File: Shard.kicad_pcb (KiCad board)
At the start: 4 copper layers, 52 parts, among them J1 USB_C_Receptacle_USB2.0_16P, J2 Conn_01x08, J3 Conn_01x08, J4 Conn_01x08, J5 Conn_01x08, SW1 SW_Push, SW2 SW_Push, U1 ESP32-S3, U2 USBLC6-2P6, U3 TLV76733DRVx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

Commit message: Finish initial PCB Layout
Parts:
- ANT1: footprint RF_Antenna:Texas_SWRA117D_2.4GHz_Left -> RF_Antenna:Texas_SWRA117D_2.4GHz_Right
- C1, C13, C15, C3, C6, C9: footprint Capacitor_SMD:C_0603_1608Metric -> Capacitor_SMD:C_0201_0603Metric
- C10, C11, C12, C16, C4, C7, C8: footprint Capacitor_SMD:C_1206_3216Metric -> Capacitor_SMD:C_0201_0603Metric
- R11: footprint Resistor_SMD:R_0805_2012Metric -> Resistor_SMD:R_0201_0603Metric
- moved J2 89.3 mm to (169.1, 81.7), turned to -20 degrees
- moved J3 87.5 mm to (168.3, 94.3), turned to -20 degrees
- moved U5 78.5 mm to (157.6, 101.0), turned to -45 degrees
- moved C16 58.2 mm to (157.3, 96.0), turned to 135 degrees
- moved Y1 57.8 mm to (151.9, 87.9), turned to -45 degrees
- moved C1 55.6 mm to (139.6, 106.7), turned to -90 degrees
- moved C20 54.9 mm to (144.4, 85.7), turned to 45 degrees
- moved R6 54.9 mm to (152.3, 97.0), turned to -45 degrees
- moved C10 54.5 mm to (148.3, 99.7), turned to -135 degrees
- moved C4 54.1 mm to (148.3, 88.6), turned to 45 degrees
- moved R7 53.6 mm to (153.4, 96.0), turned to -45 degrees
- moved R12 53.0 mm to (159.7, 95.1)
- moved R8 52.6 mm to (154.5, 94.9), turned to -45 degrees
- moved C11 52.6 mm to (151.0, 91.3), turned to 45 degrees
- moved C9 51.2 mm to (147.7, 99.1), turned to -135 degrees
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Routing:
- net VBUS: track 17.6 -> 0.00 mm
- net /D-: track 8.21 -> 0.00 mm
- net /D+: track 7.94 -> 0.00 mm
- net /D_N: track 7.79 -> 0.00 mm
- net GND: track 7.14 -> 0.00 mm, vias 1 -> 0
- net /D_P: track 7.05 -> 0.00 mm
- net Net-(J1-CC2): track 3.16 -> 0.00 mm
- net Net-(J1-CC1): track 3.16 -> 0.00 mm
- removed copper zone on F.Cu, net GND
- removed copper zone on In1.Cu, net GND

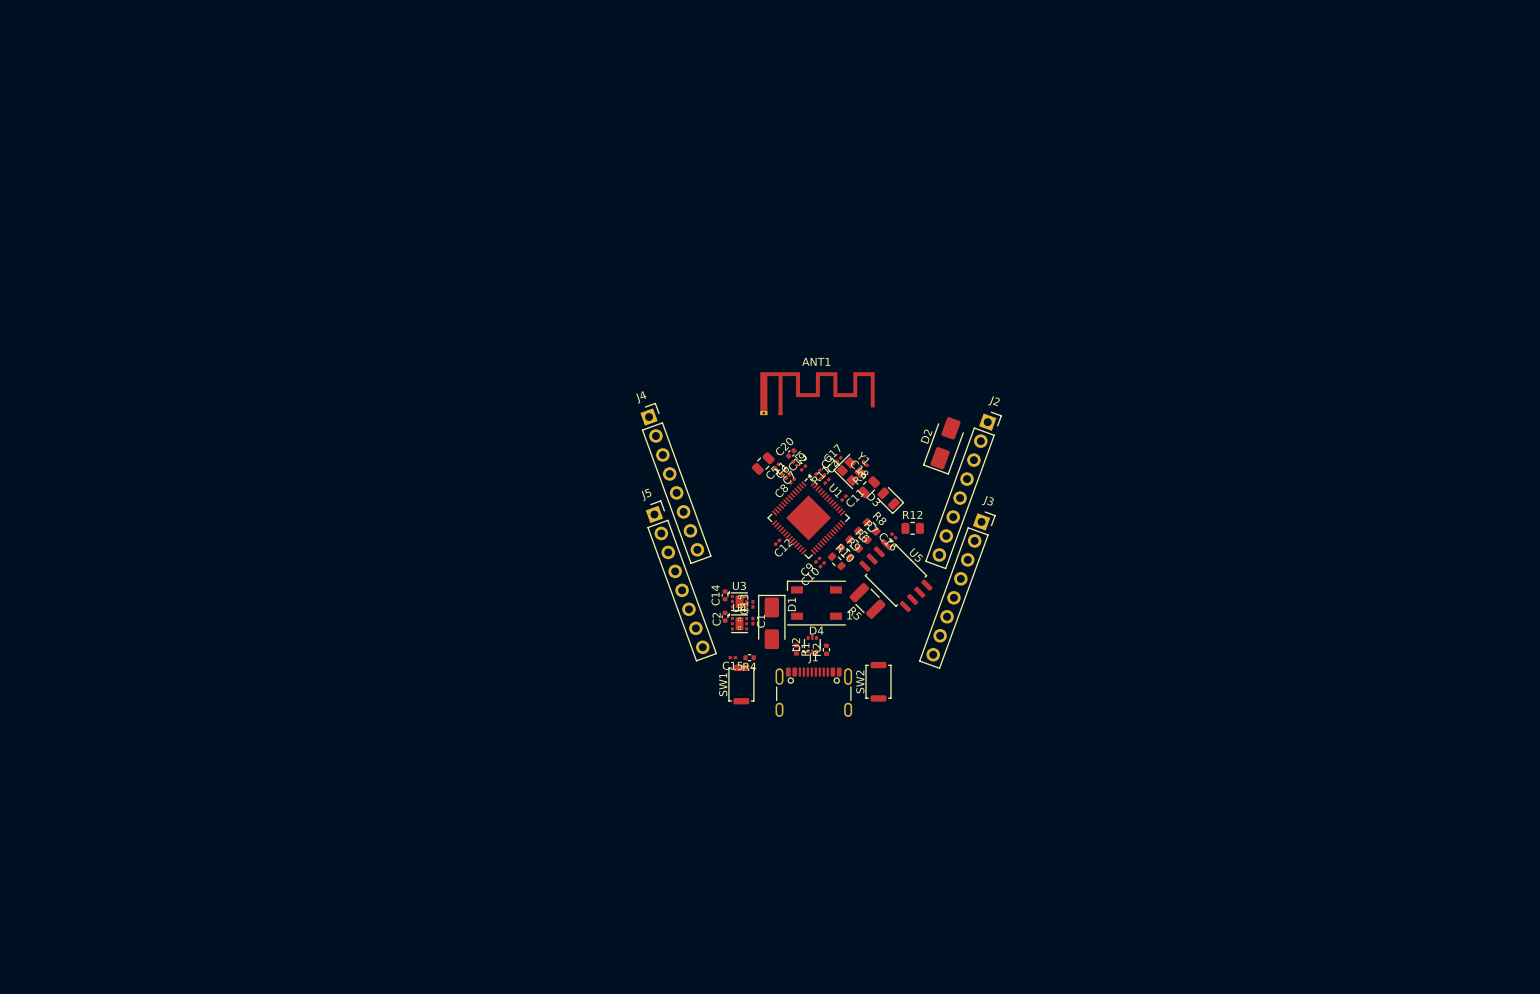
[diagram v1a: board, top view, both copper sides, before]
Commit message: Started routing USB & Power
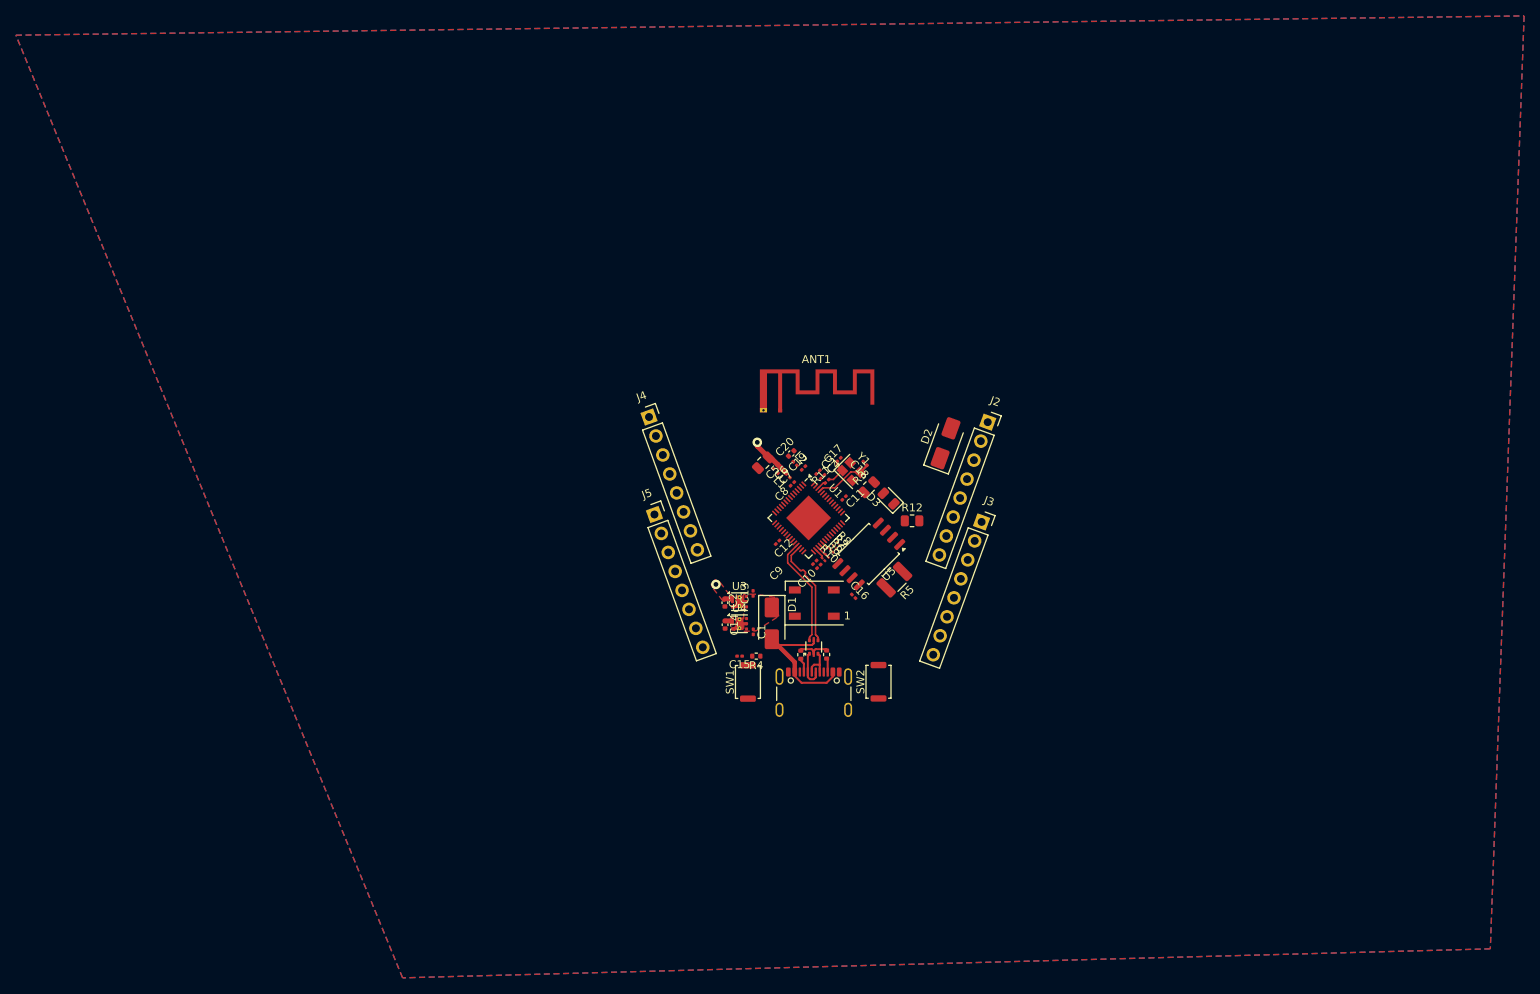
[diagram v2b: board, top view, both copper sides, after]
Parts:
- R10, R6, R7, R8, R9: footprint Resistor_SMD:R_0603_1608Metric -> Resistor_SMD:R_01005_0402Metric
- moved C16 9.12 mm to (152.2, 103.6), turned to -45 degrees
- moved R8 4.69 mm to (150.3, 97.0)
- moved U5 4.38 mm to (154.1, 98.3), turned to -135 degrees
- moved R5 4.31 mm to (157.3, 101.5), turned to -135 degrees
- moved R7 3.81 mm to (149.9, 97.5)
- moved C14 3.70 mm to (136.1, 107.2), turned to -90 degrees
- moved R6 2.95 mm to (149.5, 97.9)
- moved R9 2.36 mm to (148.9, 98.5)
- moved C2 1.77 mm to (136.0, 104.4), turned to -90 degrees
- moved R10 1.70 mm to (148.4, 99.0)
- moved C13 1.39 mm to (139.6, 103.3)
- moved C1 1.35 mm to (139.6, 108.1)
- moved R12 0.95 mm to (159.6, 94.1)
- moved SW1 0.89 mm to (138.9, 114.4)
- moved C15 0.87 mm to (137.9, 111.2)
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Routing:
- net +3.3V: track 0.00 -> 26.9 mm, vias 0 -> 2
- net VBUS: track 0.00 -> 18.7 mm
- net /D-: track 0.00 -> 13.8 mm
- net /D+: track 0.00 -> 13.8 mm
- net GND: track 0.00 -> 8.92 mm
- net /XTAL_N: track 0.00 -> 7.31 mm
- net /D_N: track 0.00 -> 4.90 mm
- net /D_P: track 0.00 -> 4.15 mm
- net Net-(C17-Pad1): track 0.00 -> 3.58 mm
- net Net-(J1-CC1): track 0.00 -> 1.86 mm
- net Net-(J1-CC2): track 0.00 -> 1.67 mm
- net /E3.3V: track 0.00 -> 1.45 mm
- net Net-(U1-SPIHD): track 0.00 -> 1.37 mm
- net Net-(U1-SPICLK): track 0.00 -> 1.34 mm
- net Net-(U1-SPIWP): track 0.00 -> 1.33 mm
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- added copper zone on F.Cu, net +3.3V
- added copper zone on F.Cu, net /VIN
- added copper zone on B.Cu, net GND
- added copper zone on F.Cu, net GND
- added copper zone on In1.Cu, net GND
- added copper zone on In2.Cu, net GND

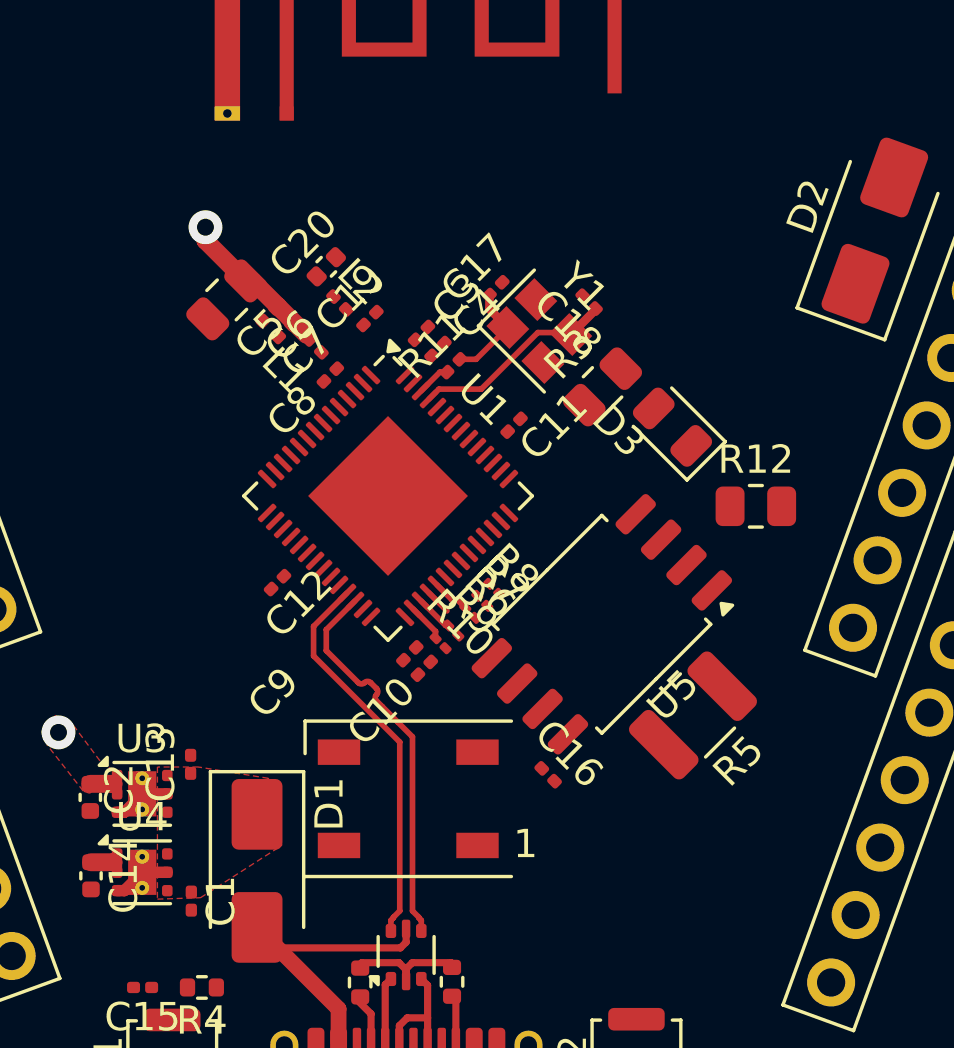
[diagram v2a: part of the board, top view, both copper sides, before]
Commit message: Completed Power routing
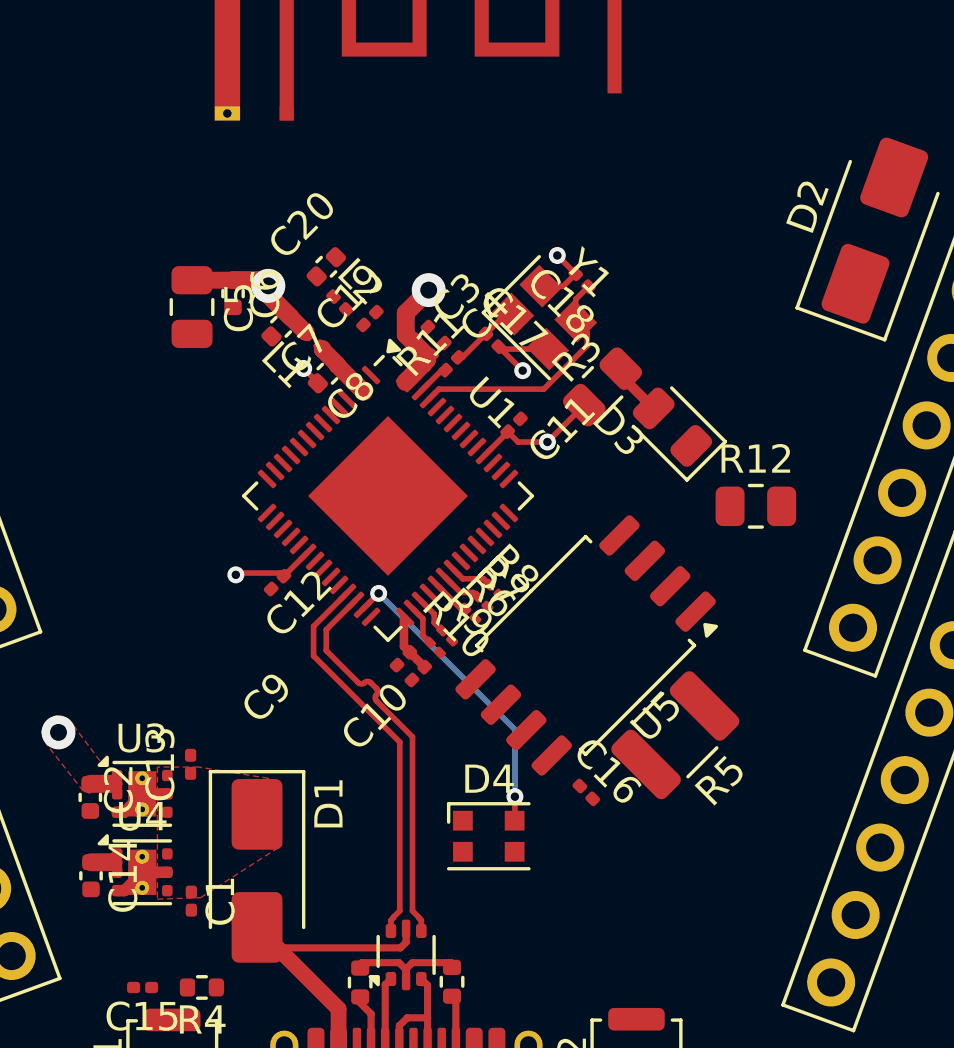
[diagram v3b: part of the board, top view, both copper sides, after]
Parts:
- C6, C7, C8: footprint Capacitor_SMD:C_0201_0603Metric -> Capacitor_SMD:C_0402_1005Metric
- D4: footprint LED_SMD:LED_WS2812B_PLCC4_5.0x5.0mm_P3.2mm -> LED_SMD:LED_WS2812B-2020_PLCC4_2.0x2.0mm
- moved D4 3.14 mm to (150.1, 105.8), turned to 0 degrees
- moved C17 1.83 mm to (150.2, 88.2), turned to -45 degrees
- moved C16 1.49 mm to (153.6, 104.2)
- moved C6 1.48 mm to (141.1, 86.6), turned to -90 degrees
- moved C5 1.25 mm to (139.6, 87.1), turned to -90 degrees
- moved U5 0.95 mm to (153.6, 99.0)
- moved R5 0.94 mm to (156.7, 102.2)
- moved C18 0.81 mm to (153.4, 86.1)
- moved Y1 0.51 mm to (152.1, 87.4)
- moved C9 0.29 mm to (147.1, 99.5)
- moved R9 0.28 mm to (148.6, 98.7)
- moved C10 0.28 mm to (147.6, 100.0)
- moved R10 0.25 mm to (148.2, 99.1)
- moved L1 0.20 mm to (143.9, 88.2)
- moved C7 0.19 mm to (142.8, 87.8)
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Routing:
- net +3.3V: track 26.9 -> 52.1 mm, vias 2 -> 5
- net /21: track 0.00 -> 10.8 mm, vias 0 -> 2
- net GND: track 8.92 -> 14.9 mm, vias 0 -> 3
- net /VDD3P3: track 0.00 -> 2.16 mm
- net /VDD_SPI: track 0.00 -> 2.05 mm
- net Net-(D3-A): track 0.00 -> 1.89 mm
- net Net-(U1-SPID): track 0.00 -> 1.52 mm
- net /XTAL_N: track 7.31 -> 8.83 mm
- net Net-(U1-SPIQ): track 0.00 -> 1.44 mm
- net Net-(C17-Pad1): track 3.58 -> 2.56 mm
- net /SPICS0: track 0.90 -> 0.00 mm

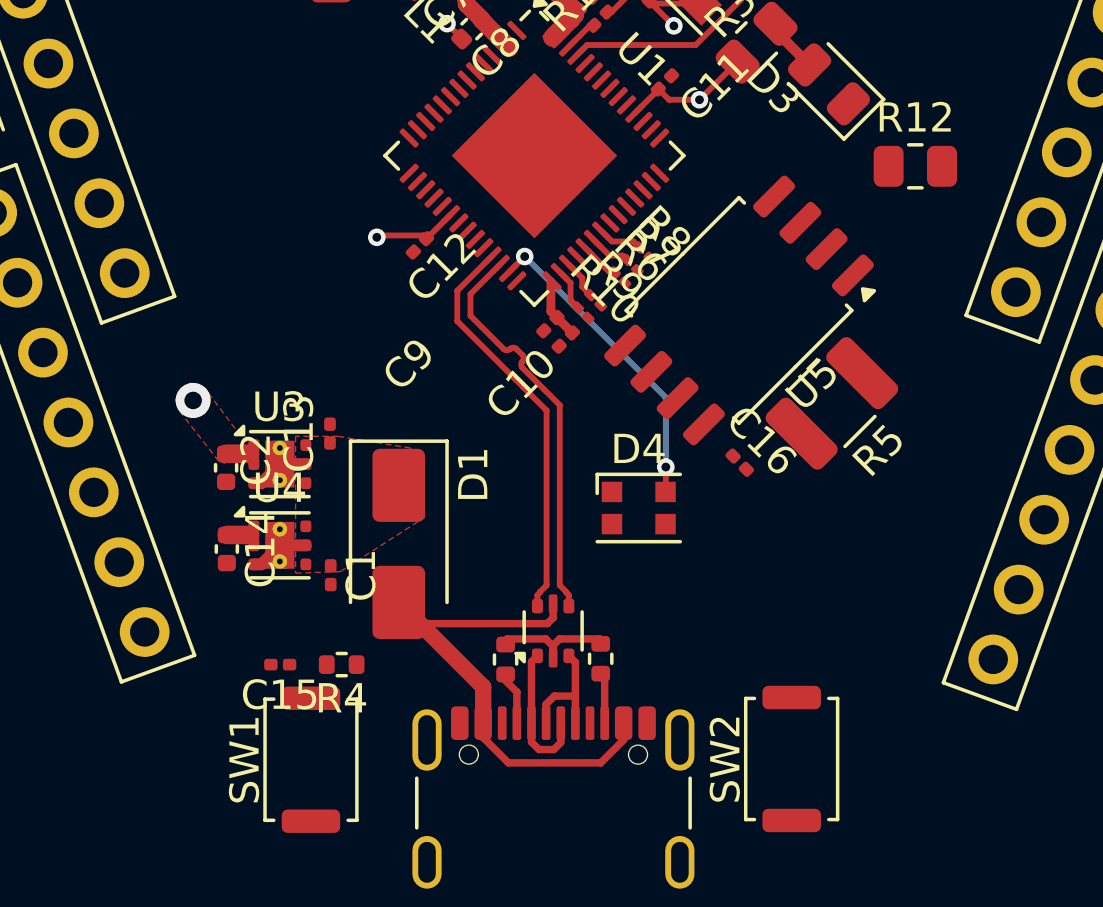
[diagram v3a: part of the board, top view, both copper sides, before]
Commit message: Routed SPI traces
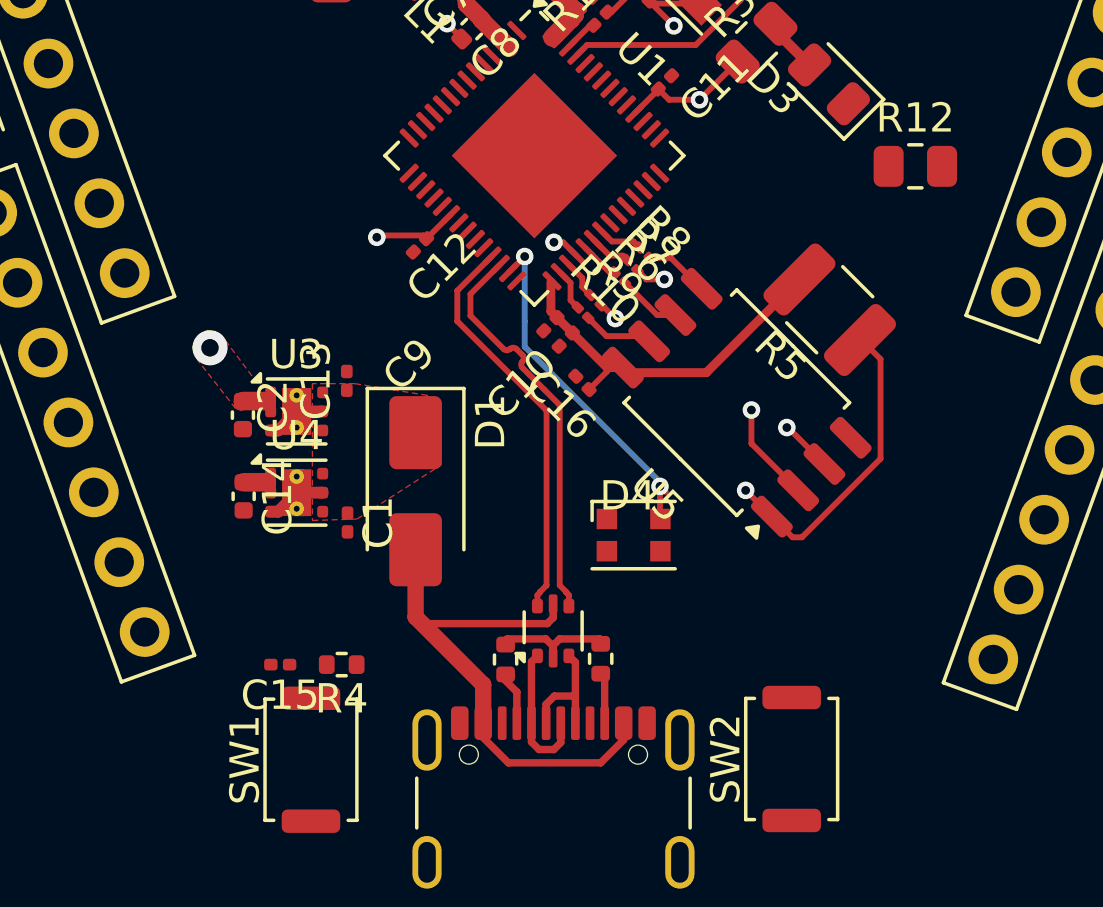
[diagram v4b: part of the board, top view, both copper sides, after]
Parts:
- moved C16 6.03 mm to (148.2, 101.5), turned to 135 degrees
- moved R5 3.20 mm to (156.7, 99.0), turned to 135 degrees
- moved U5 3.15 mm to (153.5, 102.2), turned to 135 degrees
- moved C1 1.89 mm to (140.2, 106.3)
- moved C13 1.89 mm to (140.2, 101.5)
- moved C14 1.89 mm to (136.6, 105.4)
- moved C2 1.89 mm to (136.6, 102.6)
- moved D1 1.89 mm to (142.5, 105.2)
- moved U3 1.89 mm to (138.4, 102.5)
- moved U4 1.89 mm to (138.4, 105.3)
- moved D4 0.94 mm to (149.9, 106.7)
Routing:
- net /SPICS0: track 0.00 -> 23.2 mm, vias 0 -> 2
- net /VDD_SPI: track 2.05 -> 12.8 mm
- net /SPIQ: track 0.00 -> 10.2 mm, vias 0 -> 2
- net /SPIWP: track 0.00 -> 9.91 mm, vias 0 -> 2
- net +3.3V: track 52.1 -> 49.2 mm
- net /SPIHD: track 0.00 -> 2.42 mm
- net /SPID: track 0.00 -> 2.21 mm
- net /SPICLK: track 0.00 -> 2.18 mm
- net VBUS: track 18.7 -> 20.2 mm
- net /21: track 10.8 -> 11.4 mm
